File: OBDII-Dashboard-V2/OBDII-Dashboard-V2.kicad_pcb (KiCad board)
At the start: 2 copper layers, 108 x 61.7 mm, 26 parts, among them P1 USB_C_Plug_USB2.0, SW1 BOOT, SW2 RESET, U1 LCD, U3 AMS1117-3.3, U4 BME280, U5 ESP32-S3-WROOM-1

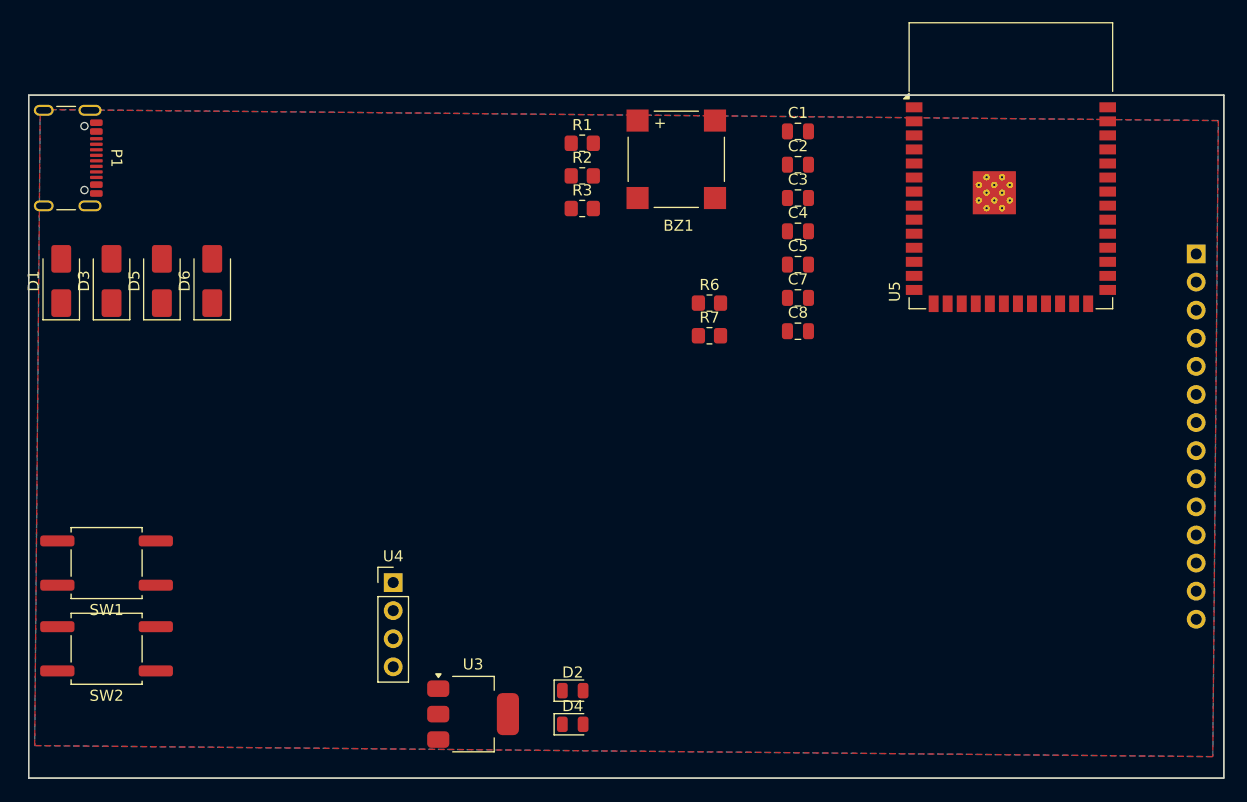
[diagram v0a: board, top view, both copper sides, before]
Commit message: updated component placement
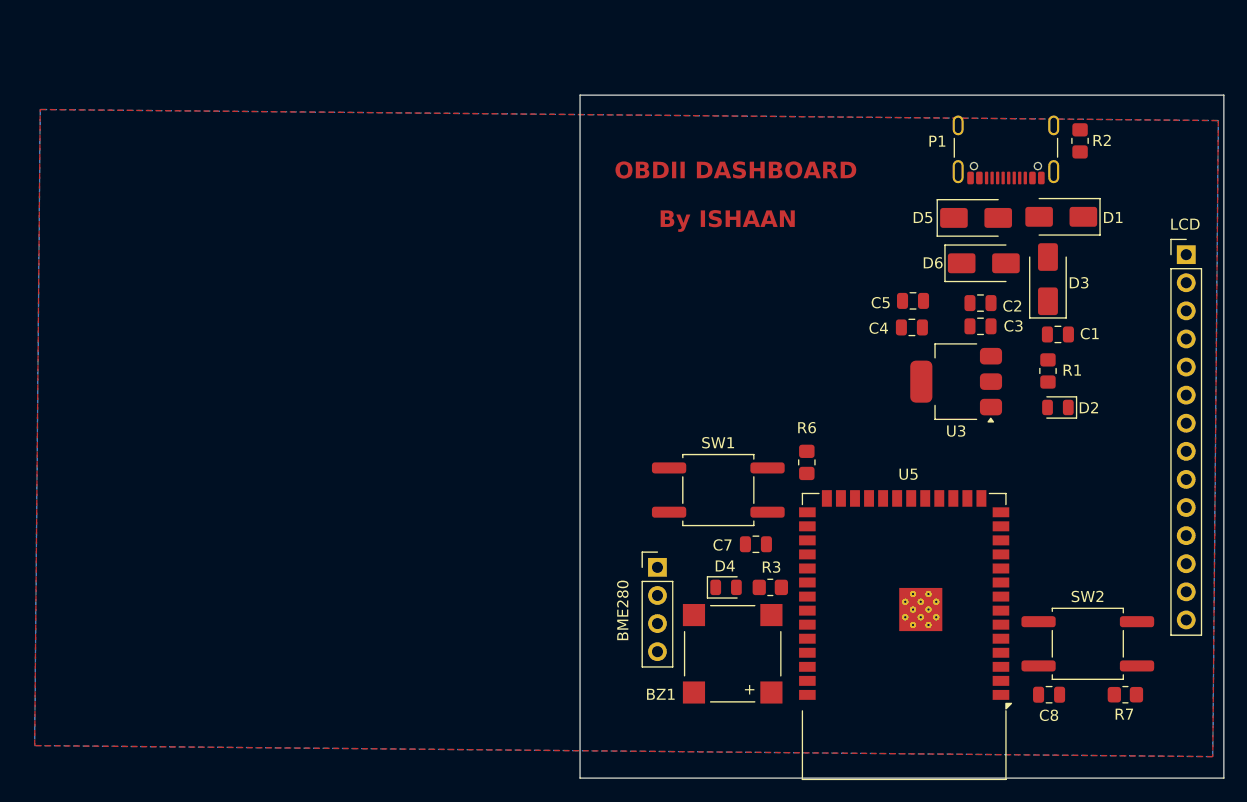
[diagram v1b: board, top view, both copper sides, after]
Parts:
- removed U4: BME280, Connector_PinHeader_2.54mm:PinHeader_1x04_P2.54mm_Vertical
- added BME280: Conn_01x04_Socket, Connector_PinHeader_2.54mm:PinHeader_1x04_P2.54mm_Vertical, F.Cu at (73.3, 61.9)
- LCD: renamed from U1; moved to F.Cu
- moved D1 90.6 mm to (109.8, 30.2), turned to 180 degrees
- moved SW2 88.7 mm to (112.2, 68.8), turned to 180 degrees
- moved P1 85.9 mm to (104.8, 23.0), turned to 180 degrees
- moved D3 84.7 mm to (108.6, 35.8)
- moved D5 73.8 mm to (102.1, 30.3), turned to 0 degrees
- moved D6 69.8 mm to (102.8, 34.4), turned to 0 degrees
- moved SW1 55.7 mm to (78.8, 54.9), turned to 180 degrees
- moved U3 53.0 mm to (100.3, 45.1), turned to 180 degrees
- moved D2 50.8 mm to (109.5, 47.4), turned to 180 degrees
- moved R7 49.7 mm to (115.6, 73.4)
- moved R1 46.9 mm to (108.6, 44.1), turned to -90 degrees
- moved R2 45.1 mm to (111.5, 23.3), turned to -90 degrees
- moved BZ1 45.0 mm to (80.1, 69.7), turned to 180 degrees
- moved U5 43.7 mm to (95.6, 68.2), turned to 180 degrees
- moved C8 39.9 mm to (108.7, 73.4)
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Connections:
- C7 pad 2: unconnected-(C7-Pad2) -> GND
- C8 pad 2: unconnected-(C8-Pad2) -> GND
- R3 pad 2: Net-(U5-IO4) -> Net-(U5-IO40)
- U5 pad 33: unconnected-(U5-IO40-Pad33) -> Net-(U5-IO40)
- U5 pad 4: Net-(U5-IO4) -> unconnected-(U5-IO4-Pad4)
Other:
- board size 108 x 61.7 mm -> 58.2 x 61.7 mm
- board text added: "By ISHAAN"
- board text added: "OBDII DASHBOARD"
